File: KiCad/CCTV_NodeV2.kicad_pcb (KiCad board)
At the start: 2 copper layers, 89.9 x 60.8 mm, 9 parts, among them J1 SOLAR, J2 BATT, U1 CN3791, U2 BMS 1S, U3 MT3608, U4 ESP32-S3, U5 OV7670

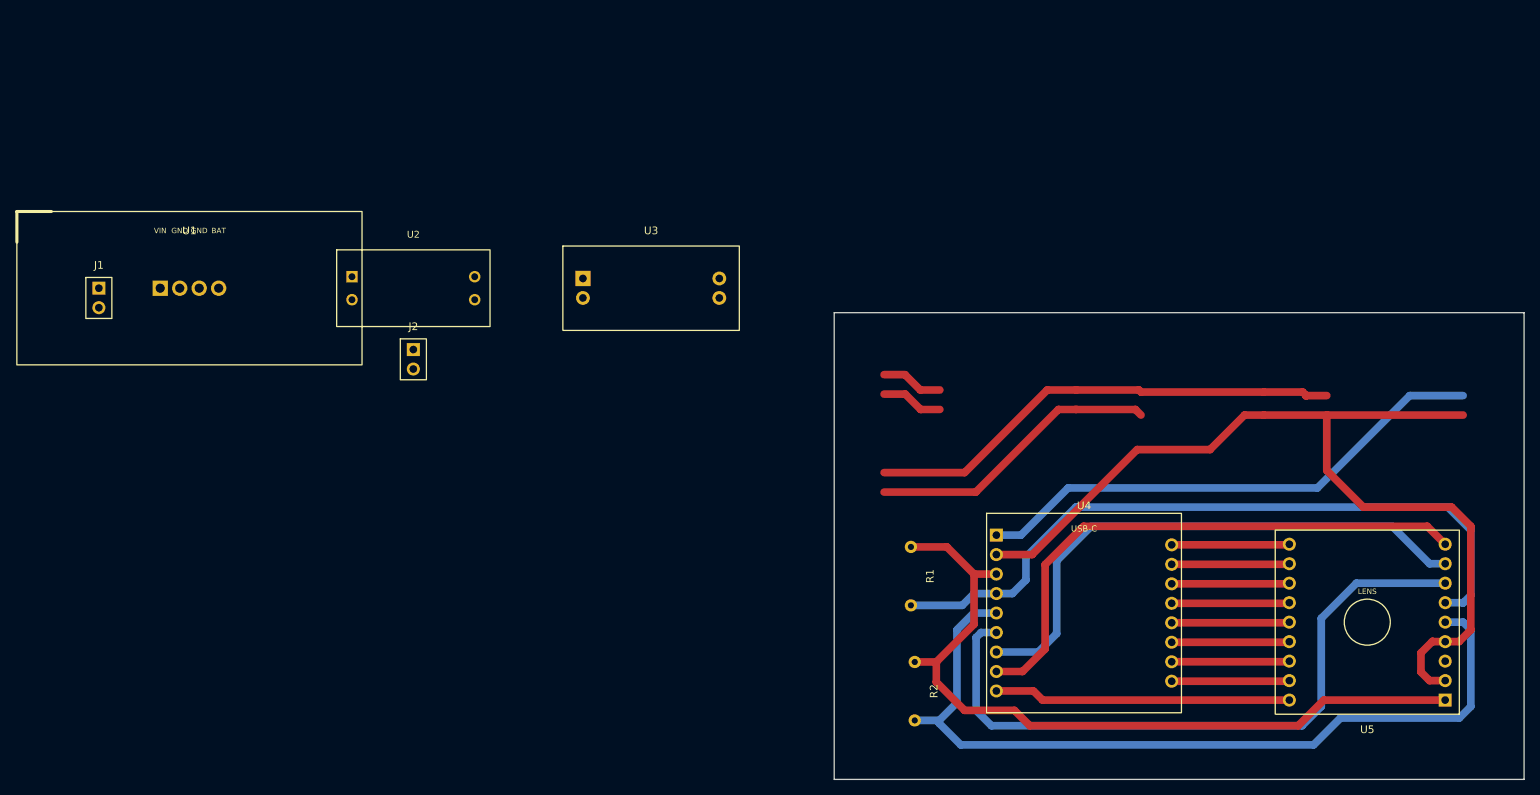
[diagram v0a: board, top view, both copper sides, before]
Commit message: Replace U2 BMS from DW01A+FS8205A to TC4056A_BMS_Module
Replaces the standalone 1S BMS (DW01A + FS8205A) with the TC4056A
combined USB charger + BMS protection module on U2.

Schematic (CCTV_NodeV2.kicad_sch):
- Added CCTV2:TC4056A_BMS lib symbol (6 pins):
    Pin 1 = IN+  (USB 5V charging input)  → NC marker
    Pin 2 = IN-  (USB GND)               → GND symbol
    Pin 3 = B+   (battery positive)       → BATT+ (same position as old BMS pin1)
    Pin 4 = B-   (battery negative)       → BATT-/GND (same position as old BMS pin2)
    Pin 5 = OUT+ (BMS protected output +) → P+    (same position as old BMS pin3)
    Pin 6 = OUT- (BMS protected output -) → PROT- (same position as old BMS pin4)
- Replaced U2 lib_id BMS_1S → TC4056A_BMS
- Updated U2 footprint: BMS_1S_DW01A_FS8205A → TC4056A_BMS_Module
- Added GND power symbol for IN- at (117.3, 60.65)
- Added no_connect flag at IN+ (117.3, 57.3)
  (connect a USB cable / J connector here for USB charging)

PCB (CCTV_NodeV2.kicad_pcb):
- Replaced entire U2 footprint block with TC4056A_BMS_Module geometry
  (26x17mm body, 6 pads single row at 2.54mm pitch)
- Pad nets: 1=NC, 2=GND, 3=BATT+, 4=BATT-, 5=P+, 6=PROT-
- Existing traces to old 4-pad BMS pads are now airwires — re-route
  with Freerouting or manually in pcbnew
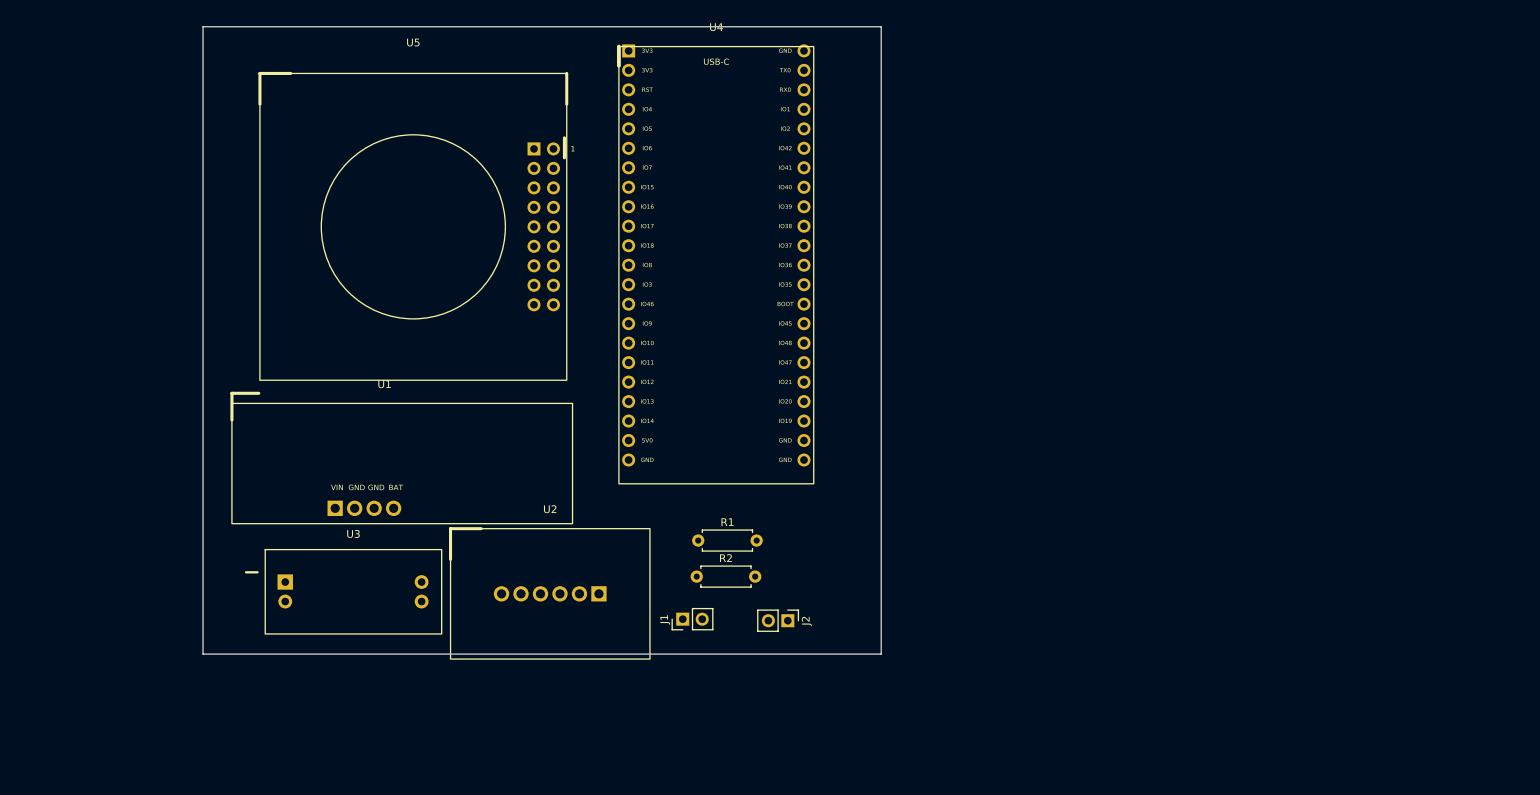
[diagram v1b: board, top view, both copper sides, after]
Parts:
- J1: value SOLAR -> Solar 6V/10W
- J2: value BATT -> Battery (ext, 2× 18650 ||)
- R1: value 4.7k -> 4.7k SIOD pull-up
- R2: value 4.7k -> 4.7k SIOC pull-up
- U2: value BMS 1S -> TC4056A_BMS; footprint CCTV_RPi4:BMS_1S_DW01A_FS8205A -> CCTV_RPi4:TC4056A_BMS_Module
- U4: value ESP32-S3 -> ESP32-S3-DevKitC-1 N16R8
- moved U5 119.1 mm to (64.0, 60.0), turned to 0 degrees
- moved J1 87.5 mm to (82.1, 111.2), turned to 90 degrees
- moved U4 66.0 mm to (86.5, 65.0)
- moved J2 60.3 mm to (95.8, 111.3), turned to -90 degrees
- moved U3 55.4 mm to (39.2, 107.6)
- moved U2 43.7 mm to (64.8, 107.8)
- moved U1 32.0 mm to (40.9, 90.2)
- moved R2 30.5 mm to (84.0, 105.6), turned to 0 degrees
- moved R1 27.7 mm to (84.1, 100.9), turned to 0 degrees
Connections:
- net SOLAR+ renamed /SOLAR+
- net SOLAR- renamed /SOLAR-
- J2 pad 2: BATT- -> /BATT-
- R1 pad 2: SIOD -> /SIOD
- R2 pad 2: SIOC -> /SIOC
- U1 pad 3: BATT- -> /BATT-
- U2 pad 1: BATT+ -> (no net)
- U2 pad 2: BATT- -> GND
- U2 pad 3: P+ -> BATT+
- U2 pad 4: GND -> /BATT-
- U3 pad 1: P+ -> /P+
- U3 pad 2: GND -> /PROT-
- U3 pad 4: GND -> /+5V_GND
- U4 pad 1: +5V -> unconnected-(U4-3V3-Pad1)
- U4 pad 10: CAM_D0 -> /HREF
- U4 pad 11: CAM_D1 -> /VSYNC
- U4 pad 12: CAM_D2 -> /SIOC
- U4 pad 13: CAM_D3 -> unconnected-(U4-GPIO3-Pad13)
- U4 pad 14: CAM_D4 -> unconnected-(U4-GPIO46-Pad14)
- U4 pad 15: CAM_D5 -> +3V3
- U4 pad 16: CAM_D6 -> GND
- U4 pad 17: CAM_D7 -> +5V
- U4 pad 2: GND -> unconnected-(U4-3V3_2-Pad2)
- U4 pad 3: +3V3 -> unconnected-(U4-RST-Pad3)
- U4 pad 4: SIOD -> unconnected-(U4-GPIO4_SIOD-Pad4)
- U4 pad 5: SIOC -> unconnected-(U4-GPIO5_SIOC-Pad5)
- U4 pad 6: VSYNC -> unconnected-(U4-GPIO6_VSYNC-Pad6)
- U4 pad 7: HREF -> unconnected-(U4-GPIO7_HREF-Pad7)
- U4 pad 8: PCLK -> /XCLK
- U4 pad 9: XCLK -> /PCLK
- U5 pad 10: XCLK -> /CAM_D6
- U5 pad 11: CAM_D7 -> /CAM_D5
- U5 pad 12: CAM_D6 -> /CAM_D4
- U5 pad 13: CAM_D5 -> /CAM_D3
- U5 pad 14: CAM_D4 -> /CAM_D2
- U5 pad 15: CAM_D3 -> /CAM_D1
- U5 pad 16: CAM_D2 -> /CAM_D0
- U5 pad 17: CAM_D1 -> unconnected-(U5-RESET-Pad17)
- U5 pad 18: CAM_D0 -> unconnected-(U5-PWDN-Pad18)
- U5 pad 3: (no net) -> /SIOC
- U5 pad 4: GND -> /SIOD
- U5 pad 5: SIOC -> /VSYNC
- U5 pad 6: SIOD -> /HREF
- U5 pad 7: VSYNC -> /PCLK
- U5 pad 8: HREF -> /XCLK
- U5 pad 9: PCLK -> /CAM_D7
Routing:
- net GND: track 124.8 -> 0.00 mm
- net SIOC: track 108.7 -> 0.00 mm
- net +3V3: track 101.6 -> 0.00 mm
- net SIOD: track 93.6 -> 0.00 mm
- net VSYNC: track 88.8 -> 0.00 mm
- net PCLK: track 73.8 -> 0.00 mm
- net HREF: track 72.9 -> 0.00 mm
- net +5V: track 68.5 -> 0.00 mm
- net BATT+: track 62.6 -> 0.00 mm
- net XCLK: track 38.7 -> 0.00 mm
- net BATT-: track 38.3 -> 0.00 mm
- net CAM_D2: track 15.4 -> 0.00 mm
- net CAM_D7: track 15.4 -> 0.00 mm
- net CAM_D6: track 15.4 -> 0.00 mm
- net CAM_D5: track 15.4 -> 0.00 mm
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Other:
- board size 89.9 x 60.8 mm -> 88.4 x 81.8 mm

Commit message: Fix U3 MT3608 pad 4: remove '+5V_GND' net, correct to GND
OUT- of a boost converter is the output return path = GND.
A net label '+5V_GND' had been placed at the MT3608 OUT- pin
position (192.7, 75.08) in the schematic, causing KiCad to create
a merged '/+5V_GND' net that incorrectly tied the +5V and GND
buses together on pad 4.

Schematic (CCTV_NodeV2.kicad_sch):
- Deleted stray net label '+5V_GND' at (192.7, 75.08)
- The GND power symbol already present at (192.7, 76.35)
  connects OUT- to GND correctly — no replacement needed

PCB (CCTV_NodeV2.kicad_pcb):
- U3 pad 4 (OUT-): net '/+5V_GND' → 'GND'
- This removes the short circuit between +5V and GND on U3
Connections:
- U3 pad 4: /+5V_GND -> GND
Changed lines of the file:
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@@
 			(layers "*.Cu" "*.Mask")
 			(remove_unused_layers no)
-			(net "/+5V_GND")
+			(net "GND")
 			(pinfunction "OUT-_4")
 			(pintype "passive")

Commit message: Fix U3 MT3608 pad 4 (OUT-): GND → PROT- (same node as pad 2 IN-)
Pad 2 (IN-) and pad 4 (OUT-) of the MT3608 module are connected
together on the module's internal copper pour — they are the SAME
electrical node. Both must be on the PROT- net so the BMS can
actually cut off the load when over-discharge occurs.

Previously pad 4 was changed to GND in the last commit, which would
have shorted the BMS protection FETs (PROT- → GND directly) and
made the DW01A protection circuit useless.

Correct circuit:
  Battery B- → BMS B- → [DW01A FETs] → PROT- → MT3608 pad2(IN-)
                                                         ↕ (same node on module PCB)
                                               PROT- → MT3608 pad4(OUT-)
                                                         ↓
                                               PROT- → ESP32 GND / all load GND

When BMS trips at ~2.4V: PROT- floats → MT3608 loses return path
→ output collapses → ESP32 off. ✓

Schematic: replaced GND power symbol at MT3608 OUT- with PROT- label
PCB: U3 pad 4 net GND → /PROT-
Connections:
- U3 pad 4: GND -> /PROT-
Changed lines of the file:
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@@
 			(layers "*.Cu" "*.Mask")
 			(remove_unused_layers no)
-			(net "GND")
+			(net "/PROT-")
 			(pinfunction "OUT-_4")
 			(pintype "passive")

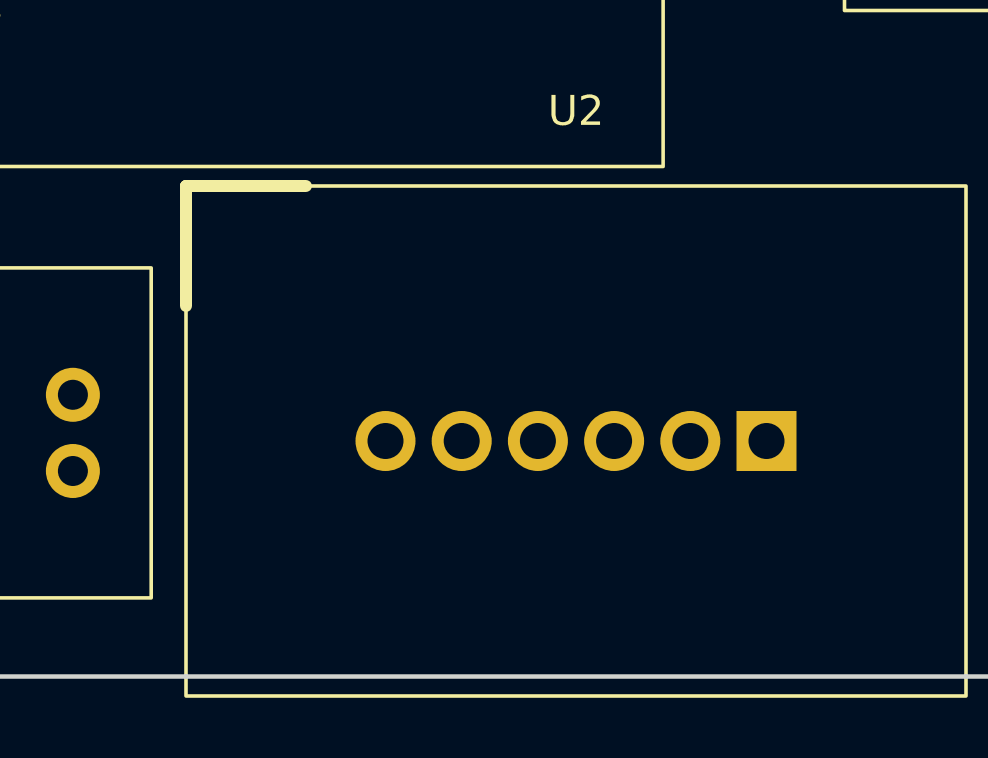
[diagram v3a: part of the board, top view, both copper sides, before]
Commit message: Fix TC4056A BMS footprint: 4 pads at BOTTOM EDGE, 4-pin symbol
Physical module (from image): 26x17mm PCB, USB-C charging at top,
4 through-hole solder pads at the BOTTOM EDGE (not in the middle).
Pad order left-to-right: OUT- | B- | B+ | OUT+

TC4056A_BMS_Module.kicad_mod:
- Removed 6 centre pads (IN+/IN- are USB-C handled internally)
- 4 pads repositioned at bottom edge y=+7.5:
    Pad 1 (OUT-/PROT-) : x=-6.75  [square, pin 1 marker]
    Pad 2 (B- /BATT-)  : x=-2.25
    Pad 3 (B+ /BATT+)  : x=+2.25
    Pad 4 (OUT+/P+)    : x=+6.75
- USB-C placeholder at top, IC boxes, LED circles on F.Fab
- Pad spacing ~4.5mm (verify against your specific module)

CCTV_NodeV2.kicad_sch:
- TC4056A_BMS symbol simplified to 4 pins (removed IN+/IN-)
    Pin 1 = B+   → BATT+
    Pin 2 = B-   → BATT-
    Pin 3 = OUT+ → P+
    Pin 4 = OUT- → PROT-
- Removed IN- GND power symbol at (117.3, 60.65)
- Removed IN+ no-connect flag at (117.3, 57.3)

CCTV_NodeV2.kicad_pcb:
- U2 embedded footprint updated with 4-pad bottom-edge geometry
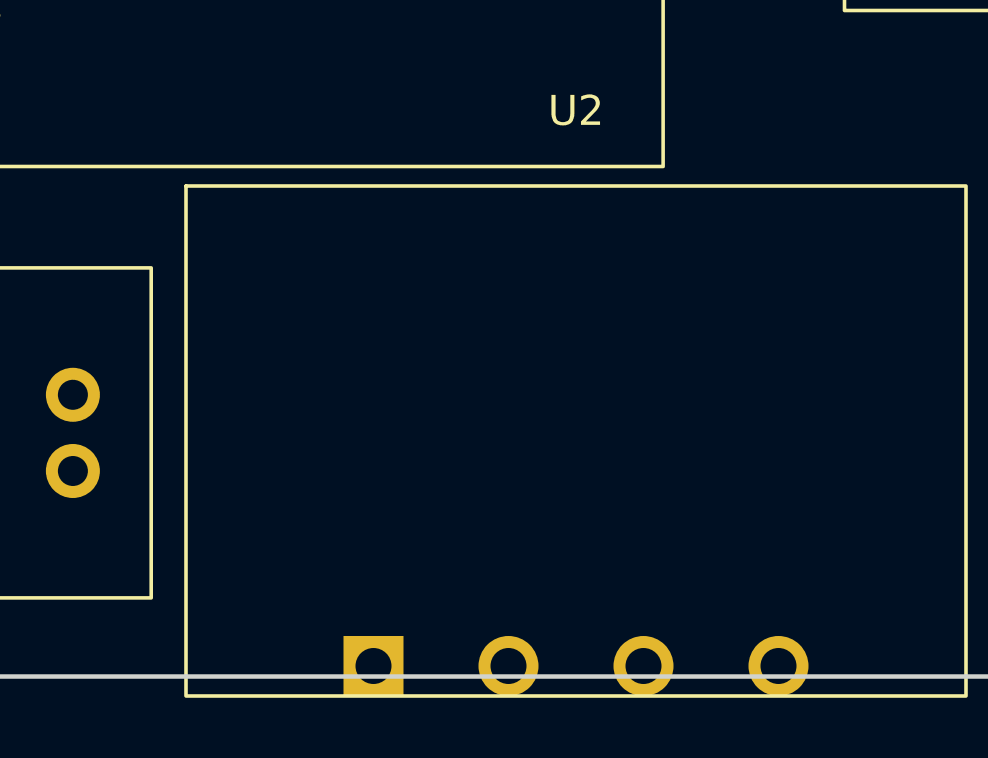
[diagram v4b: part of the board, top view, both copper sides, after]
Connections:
- U2 pad 1: (no net) -> /PROT-
- U2 pad 2: GND -> /BATT-
- U2 pad 4: /BATT- -> /P+
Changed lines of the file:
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@@
 		(layer "F.Cu")
 		(at 64.85 107.85)
-		(descr "TC4056A (TP4056) Li-Ion charger + BMS protection module. 6 pads single row 2.54mm pitch. 1=IN+ 2=IN- 3=B+ 4=B- 5=OUT+ 6=OUT-")
-		(tags "TC4056A TP4056 BMS module")
+		(descr "TC4056A BMS module 26x17mm. USB-C top. 4 pads at BOTTOM EDGE: 1=OUT-/PROT-, 2=B-/BATT-, 3=B+/BATT+, 4=OUT+/P+")
+		(tags "TC4056A TP4056 BMS module USB-C")
 		(property "Reference" "U2"
 			(at 0 -11 0)
@@
 		(attr through_hole)
 		(duplicate_pad_numbers_are_jumpers no)
-		(fp_rect
-			(start -13 -8.5) (end 13 8.5)
-			(stroke (width 0.12) (type solid))
-			(fill no)
+		(fp_rect (start -13 -8.5) (end 13 8.5)
+			(stroke (width 0.12) (type solid)) (fill no)
 			(layer "F.SilkS")
 		)
-		(fp_rect
-			(start -13 -8.5) (end 13 8.5)
-			(stroke (width 0.1) (type solid))
-			(fill no)
-			(layer "F.Fab")
-		)
-		(fp_rect
-			(start -13.7 -9.2) (end 13.7 9.2)
-			(stroke (width 0.05) (type solid))
-			(fill no)
-			(layer "F.CrtYd")
-		)
-		(fp_line
-			(start -13 -8.5) (end -13 -4.5)
-			(stroke (width 0.4) (type solid))
-			(layer "F.SilkS")
-		)
-		(fp_line
-			(start -13 -8.5) (end -9 -8.5)
-			(stroke (width 0.4) (type solid))
-			(layer "F.SilkS")
-		)
-		(fp_rect (start -10 -5.5) (end -4 5.5)
-			(stroke (width 0.15) (type solid)) (fill no)
-			(layer "F.Fab")
-		)
-		(fp_text user "USB"
-			(at -7 0 0) (layer "F.Fab")
-			(effects (font (size 0.8 0.8) (bold yes) (thickness 0.12)))
-		)
-		(fp_rect (start -2 -4) (end 2 4)
+		(fp_rect (start -13 -8.5) (end 13 8.5)
 			(stroke (width 0.1) (type solid)) (fill no)
 			(layer "F.Fab")
 		)
-		(fp_text user "4056A"
-			(at 0 0 0) (layer "F.Fab")
-			(effects (font (size 0.7 0.7) (bold yes) (thickness 0.1)))
+		(fp_rect (start -13.7 -9.2) (end 13.7 9.2)
+			(stroke (width 0.05) (type solid)) (fill no)
+			(layer "F.CrtYd")
 		)
-		(fp_rect (start 4 -4) (end 8 4)
-			(stroke (width 0.1) (type solid)) (fill no)
+		(fp_rect (start -4 -6) (end 4 -1)
+			(stroke (width 0.2) (type solid)) (fill no)
 			(layer "F.Fab")
 		)
+		(fp_text user "USB-C"
+			(at 0 -3.5 0) (layer "F.Fab")
+			(effects (font (size 0.9 0.9) (bold yes) (thickness 0.14)))
+		)
+		(fp_text user "4056A"
+			(at -3 1.75 0) (layer "F.Fab")
+			(effects (font (size 0.65 0.65) (bold yes) (thickness 0.1)))
+		)
 		(fp_text user "BMS"
-			(at 6 0 0) (layer "F.Fab")
+			(at 3.5 1.75 0) (layer "F.Fab")
 			(effects (font (size 0.65 0.65) (bold yes) (thickness 0.1)))
 		)
 		(pad "1" thru_hole rect
-			(at 6.35 0)
-			(size 2.0 2.0)
-			(drill 1.2)
+			(at -6.75 7.5)
+			(size 2.0 2.0) (drill 1.2)
 			(layers "*.Cu" "*.Mask")
 			(remove_unused_layers no)
+			(net "/PROT-")
 		)
 		(pad "2" thru_hole circle
-			(at 3.81 0)
-			(size 2.0 2.0)
-			(drill 1.2)
+			(at -2.25 7.5)
+			(size 2.0 2.0) (drill 1.2)
 			(layers "*.Cu" "*.Mask")
 			(remove_unused_layers no)
-			(net "GND")
+			(net "/BATT-")
 		)
 		(pad "3" thru_hole circle
-			(at 1.27 0)
-			(size 2.0 2.0)
-			(drill 1.2)
+			(at 2.25 7.5)
+			(size 2.0 2.0) (drill 1.2)
 			(layers "*.Cu" "*.Mask")
 			(remove_unused_layers no)
@@
 		)
 		(pad "4" thru_hole circle
-			(at -1.27 0)
-			(size 2.0 2.0)
-			(drill 1.2)
-			(layers "*.Cu" "*.Mask")
-			(remove_unused_layers no)
-			(net "/BATT-")
-		)
-		(pad "5" thru_hole circle
-			(at -3.81 0)
-			(size 2.0 2.0)
-			(drill 1.2)
+			(at 6.75 7.5)
+			(size 2.0 2.0) (drill 1.2)
 			(layers "*.Cu" "*.Mask")
 			(remove_unused_layers no)
 			(net "/P+")
 		)
-		(pad "6" thru_hole circle
-			(at -6.35 0)
-			(size 2.0 2.0)
-			(drill 1.2)
-			(layers "*.Cu" "*.Mask")
-			(remove_unused_layers no)
-			(net "/PROT-")
-		)
 		(embedded_fonts no)
